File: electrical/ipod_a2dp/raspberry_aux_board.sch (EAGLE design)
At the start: 12 parts, among them IC1 74LS244N

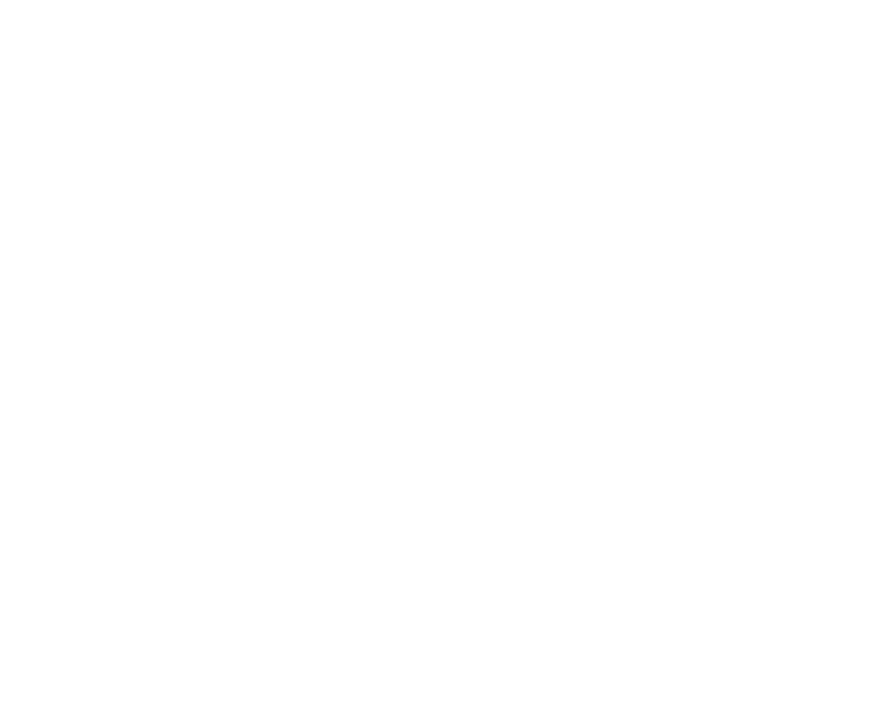
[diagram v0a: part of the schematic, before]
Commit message: more changes. proto tested. working for audio.
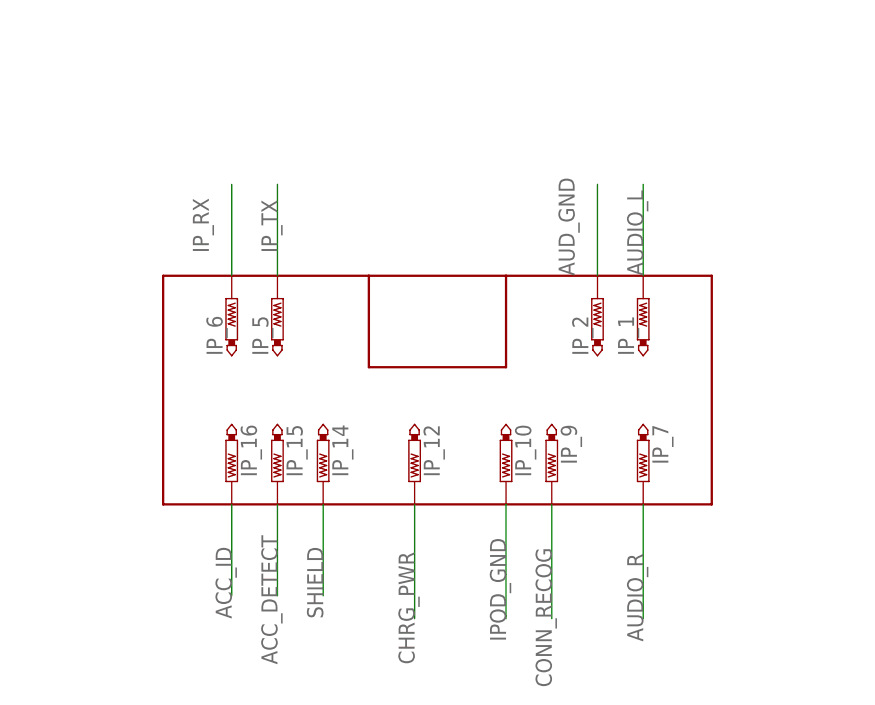
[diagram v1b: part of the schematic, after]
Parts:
- added IP_1, IP_10, IP_12, IP_14, IP_15, IP_16, IP_2, IP_5, IP_6, IP_7, IP_9: PTR1PAD1-17, testpad:PTR1PAD1-17
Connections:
- new net ACC_DETECT: IP_15.TP
- new net ACC_ID: IP_16.TP
- new net AUD_GND: IP_2.TP
- new net CHRG_PWR: IP_12.TP
- new net CONN_RECOG: IP_9.TP
- new net IPOD_GND: IP_10.TP
- new net IP_RX: IP_6.TP
- new net IP_TX: IP_5.TP
- new net SHIELD: IP_14.TP
- net AUDIO_L: now also IP_1.TP
- net AUDIO_R: now also IP_7.TP
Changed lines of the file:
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@@
 <part name="GND8" library="supply1" library_urn="urn:adsk.eagle:library:371" deviceset="GND" device=""/>
 <part name="GND9" library="supply1" library_urn="urn:adsk.eagle:library:371" deviceset="GND" device=""/>
+<part name="IP_16" library="testpad" library_urn="urn:adsk.eagle:library:385" deviceset="PTR1" device="PAD1-17" package3d_urn="urn:adsk.eagle:package:27949/1"/>
+<part name="IP_15" library="testpad" library_urn="urn:adsk.eagle:library:385" deviceset="PTR1" device="PAD1-17" package3d_urn="urn:adsk.eagle:package:27949/1"/>
+<part name="IP_6" library="testpad" library_urn="urn:adsk.eagle:library:385" deviceset="PTR1" device="PAD1-17" package3d_urn="urn:adsk.eagle:package:27949/1"/>
+<part name="IP_14" library="testpad" library_urn="urn:adsk.eagle:library:385" deviceset="PTR1" device="PAD1-17" package3d_urn="urn:adsk.eagle:package:27949/1"/>
+<part name="IP_5" library="testpad" library_urn="urn:adsk.eagle:library:385" deviceset="PTR1" device="PAD1-17" package3d_urn="urn:adsk.eagle:package:27949/1"/>
+<part name="IP_10" library="testpad" library_urn="urn:adsk.eagle:library:385" deviceset="PTR1" device="PAD1-17" package3d_urn="urn:adsk.eagle:package:27949/1"/>
+<part name="IP_12" library="testpad" library_urn="urn:adsk.eagle:library:385" deviceset="PTR1" device="PAD1-17" package3d_urn="urn:adsk.eagle:package:27949/1"/>
+<part name="IP_2" library="testpad" library_urn="urn:adsk.eagle:library:385" deviceset="PTR1" device="PAD1-17" package3d_urn="urn:adsk.eagle:package:27949/1"/>
+<part name="IP_1" library="testpad" library_urn="urn:adsk.eagle:library:385" deviceset="PTR1" device="PAD1-17" package3d_urn="urn:adsk.eagle:package:27949/1"/>
+<part name="IP_9" library="testpad" library_urn="urn:adsk.eagle:library:385" deviceset="PTR1" device="PAD1-17" package3d_urn="urn:adsk.eagle:package:27949/1"/>
+<part name="IP_7" library="testpad" library_urn="urn:adsk.eagle:library:385" deviceset="PTR1" device="PAD1-17" package3d_urn="urn:adsk.eagle:package:27949/1"/>
 </parts>
 <sheets>
 <sheet>
 <plain>
+<wire x1="20.32" y1="-22.86" x2="20.32" y2="-48.26" width="0.254" layer="94"/>
+<wire x1="20.32" y1="-48.26" x2="81.28" y2="-48.26" width="0.254" layer="94"/>
+<wire x1="81.28" y1="-48.26" x2="81.28" y2="-22.86" width="0.254" layer="94"/>
+<wire x1="81.28" y1="-22.86" x2="58.42" y2="-22.86" width="0.254" layer="94"/>
+<wire x1="58.42" y1="-22.86" x2="43.18" y2="-22.86" width="0.254" layer="94"/>
+<wire x1="43.18" y1="-22.86" x2="20.32" y2="-22.86" width="0.254" layer="94"/>
+<wire x1="43.18" y1="-33.02" x2="58.42" y2="-33.02" width="0.254" layer="94"/>
+<wire x1="58.42" y1="-33.02" x2="58.42" y2="-22.86" width="0.254" layer="94"/>
+<wire x1="43.18" y1="-33.02" x2="43.18" y2="-22.86" width="0.254" layer="94"/>
 </plain>
 <instances>
@@
 <instance part="GND9" gate="1" x="175.26" y="20.32" smashed="yes">
 <attribute name="VALUE" x="172.72" y="17.78" size="1.778" layer="96"/>
+</instance>
+<instance part="IP_16" gate="G$1" x="27.94" y="-45.72" smashed="yes" rot="R180">
+<attribute name="NAME" x="28.956" y="-39.37" size="1.778" layer="95" rot="R270"/>
+<attribute name="TP_SIGNAL_NAME" x="26.67" y="-43.18" size="1.778" layer="97" rot="R180"/>
+</instance>
+<instance part="IP_15" gate="G$1" x="33.02" y="-45.72" smashed="yes" rot="R180">
+<attribute name="NAME" x="34.036" y="-39.37" size="1.778" layer="95" rot="R270"/>
+<attribute name="TP_SIGNAL_NAME" x="31.75" y="-43.18" size="1.778" layer="97" rot="R180"/>
+</instance>
+<instance part="IP_6" gate="G$1" x="27.94" y="-25.4" smashed="yes">
+<attribute name="NAME" x="26.924" y="-31.75" size="1.778" layer="95" rot="R90"/>
+<attribute name="TP_SIGNAL_NAME" x="29.21" y="-27.94" size="1.778" layer="97"/>
+</instance>
+<instance part="IP_14" gate="G$1" x="38.1" y="-45.72" smashed="yes" rot="R180">
+<attribute name="NAME" x="39.116" y="-39.37" size="1.778" layer="95" rot="R270"/>
+<attribute name="TP_SIGNAL_NAME" x="36.83" y="-43.18" size="1.778" layer="97" rot="R180"/>
+</instance>
+<instance part="IP_5" gate="G$1" x="33.02" y="-25.4" smashed="yes">
+<attribute name="NAME" x="32.004" y="-31.75" size="1.778" layer="95" rot="R90"/>
+<attribute name="TP_SIGNAL_NAME" x="34.29" y="-27.94" size="1.778" layer="97"/>
+</instance>
+<instance part="IP_10" gate="G$1" x="58.42" y="-45.72" smashed="yes" rot="R180">
+<attribute name="NAME" x="59.436" y="-39.37" size="1.778" layer="95" rot="R270"/>
+<attribute name="TP_SIGNAL_NAME" x="57.15" y="-43.18" size="1.778" layer="97" rot="R180"/>
+</instance>
+<instance part="IP_12" gate="G$1" x="48.26" y="-45.72" smashed="yes" rot="R180">
+<attribute name="NAME" x="49.276" y="-39.37" size="1.778" layer="95" rot="R270"/>
+<attribute name="TP_SIGNAL_NAME" x="46.99" y="-43.18" size="1.778" layer="97" rot="R180"/>
+</instance>
+<instance part="IP_2" gate="G$1" x="68.58" y="-25.4" smashed="yes">
+<attribute name="NAME" x="67.564" y="-31.75" size="1.778" layer="95" rot="R90"/>
+<attribute name="TP_SIGNAL_NAME" x="69.85" y="-27.94" size="1.778" layer="97"/>
+</instance>
+<instance part="IP_1" gate="G$1" x="73.66" y="-25.4" smashed="yes">
+<attribute name="NAME" x="72.644" y="-31.75" size="1.778" layer="95" rot="R90"/>
+<attribute name="TP_SIGNAL_NAME" x="74.93" y="-27.94" size="1.778" layer="97"/>
+</instance>
+<instance part="IP_9" gate="G$1" x="63.5" y="-45.72" smashed="yes" rot="R180">
+<attribute name="NAME" x="64.516" y="-39.37" size="1.778" layer="95" rot="R270"/>
+<attribute name="TP_SIGNAL_NAME" x="62.23" y="-43.18" size="1.778" layer="97" rot="R180"/>
+</instance>
+<instance part="IP_7" gate="G$1" x="73.66" y="-45.72" smashed="yes" rot="R180">
+<attribute name="NAME" x="74.676" y="-39.37" size="1.778" layer="95" rot="R270"/>
+<attribute name="TP_SIGNAL_NAME" x="72.39" y="-43.18" size="1.778" layer="97" rot="R180"/>
 </instance>
 </instances>
@@
 <junction x="175.26" y="45.72"/>
 </segment>
+<segment>
+<pinref part="IP_1" gate="G$1" pin="TP"/>
+<wire x1="73.66" y1="-22.86" x2="73.66" y2="-12.7" width="0.1524" layer="91"/>
+<label x="73.66" y="-22.86" size="1.778" layer="95" rot="R90"/>
+</segment>
 </net>
 <net name="AUDIO_R" class="0">
@@
 <junction x="167.64" y="38.1"/>
 </segment>
-</net>
+<segment>
+<pinref part="IP_7" gate="G$1" pin="TP"/>
+<wire x1="73.66" y1="-48.26" x2="73.66" y2="-60.96" width="0.1524" layer="91"/>
+<label x="73.66" y="-63.5" size="1.778" layer="95" rot="R90"/>
+</segment>
+</net>
+<net name="AUD_GND" class="0">
+<segment>
+<pinref part="IP_2" gate="G$1" pin="TP"/>
+<wire x1="68.58" y1="-22.86" x2="68.58" y2="-12.7" width="0.1524" layer="91"/>
+<label x="66.04" y="-22.86" size="1.778" layer="95" rot="R90"/>
+</segment>
+</net>
+<net name="IP_TX" class="0">
+<segment>
+<pinref part="IP_5" gate="G$1" pin="TP"/>
+<wire x1="33.02" y1="-22.86" x2="33.02" y2="-12.7" width="0.1524" layer="91"/>
+<label x="33.02" y="-20.32" size="1.778" layer="95" rot="R90"/>
+</segment>
+</net>
+<net name="IP_RX" class="0">
+<segment>
+<pinref part="IP_6" gate="G$1" pin="TP"/>
+<wire x1="27.94" y1="-22.86" x2="27.94" y2="-12.7" width="0.1524" layer="91"/>
+<label x="25.4" y="-20.32" size="1.778" layer="95" rot="R90"/>
+</segment>
+</net>
+<net name="ACC_ID" class="0">
+<segment>
+<pinref part="IP_16" gate="G$1" pin="TP"/>
+<wire x1="27.94" y1="-48.26" x2="27.94" y2="-58.42" width="0.1524" layer="91"/>
+<label x="27.94" y="-60.96" size="1.778" layer="95" rot="R90"/>
+</segment>
+</net>
+<net name="ACC_DETECT" class="0">
+<segment>
+<pinref part="IP_15" gate="G$1" pin="TP"/>
+<wire x1="33.02" y1="-48.26" x2="33.02" y2="-58.42" width="0.1524" layer="91"/>
+<label x="33.02" y="-66.04" size="1.778" layer="95" rot="R90"/>
+</segment>
+</net>
+<net name="SHIELD" class="0">
+<segment>
+<pinref part="IP_14" gate="G$1" pin="TP"/>
+<wire x1="38.1" y1="-48.26" x2="38.1" y2="-58.42" width="0.1524" layer="91"/>
+<label x="38.1" y="-60.96" size="1.778" layer="95" rot="R90"/>
+</segment>
+</net>
+<net name="CHRG_PWR" class="0">
+<segment>
+<pinref part="IP_12" gate="G$1" pin="TP"/>
+<wire x1="48.26" y1="-48.26" x2="48.26" y2="-60.96" width="0.1524" layer="91"/>
+<label x="48.26" y="-66.04" size="1.778" layer="95" rot="R90"/>
+</segment>
+</net>
+<net name="IPOD_GND" class="0">
+<segment>
+<pinref part="IP_10" gate="G$1" pin="TP"/>
+<wire x1="58.42" y1="-48.26" x2="58.42" y2="-60.96" width="0.1524" layer="91"/>
+<label x="58.42" y="-63.5" size="1.778" layer="95" rot="R90"/>
+</segment>
+</net>
+<net name="CONN_RECOG" class="0">
+<segment>
+<pinref part="IP_9" gate="G$1" pin="TP"/>
+<wire x1="63.5" y1="-48.26" x2="63.5" y2="-60.96" width="0.1524" layer="91"/>
+<label x="63.5" y="-68.58" size="1.778" layer="95" rot="R90"/>
+</segment>
+</net>
